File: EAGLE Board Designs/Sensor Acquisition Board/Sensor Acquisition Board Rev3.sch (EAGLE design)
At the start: 79 parts, among them J1 CONNECTOR-AVR-ISP__, J2 CONNECTOR-SENSOR_NF_S_RA_BLACK, J3 CONNECTOR-SENSOR_NF_S_RA_BLACK, J4 CONNECTOR-SENSOR_NF_S_RA_BLACK, J5 CONNECTOR-SENSOR_NF_S_RA_BLACK, J6 CONNECTOR-CAN_NF_S_RA_BLACK, U1 LM340, U10 OPAMP_1_CHANNEL_OPA991, U11 OPAMP_1_CHANNEL_OPA991, U12 OPAMP_1_CHANNEL_OPA991, U13 OPAMP_1_CHANNEL_OPA991, U2 ATMEGA328P-AU, U3 MCP2515, U4 MCP3204, U5 CAN_TRANSCIEVER_TCAN1051HQV-Q1, U6 MAX7400, U7 MAX7400, U8 MAX7400, U9 MAX7400, X1 CRYSTAL16MHZ, X2 CRYSTAL16MHZ

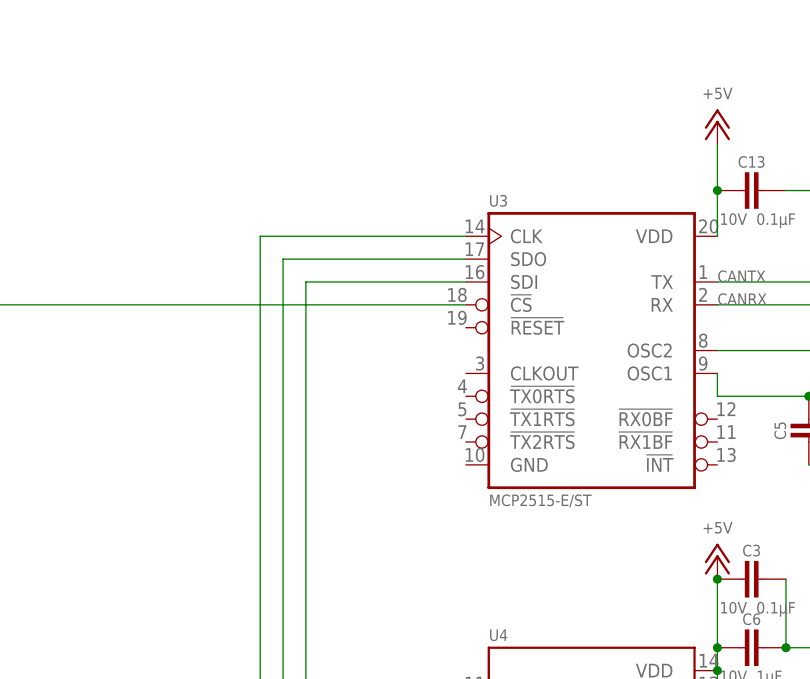
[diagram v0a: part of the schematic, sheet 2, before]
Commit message: Fixed resetlow on MCP2515
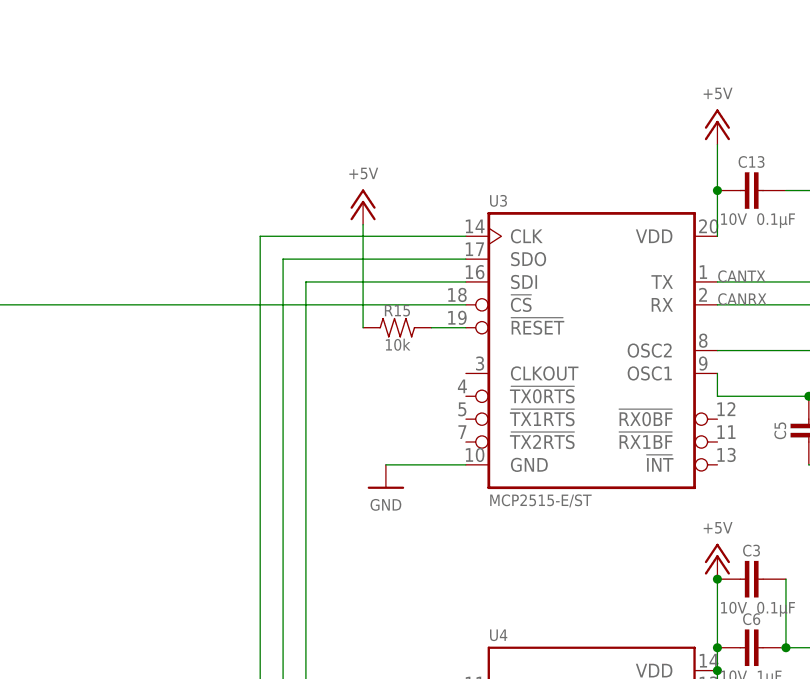
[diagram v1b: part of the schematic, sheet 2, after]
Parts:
- added R15: RESISTOR_0603_10K, HyTechDevices:RESISTOR_0603_10K
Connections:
- new net N$5: R15.2, U3.!RESET
- net +5V: now also R15.1
- net GND: now also U3.GND
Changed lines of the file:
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@@
 <part name="GND12" library="HyTechSupplies" deviceset="GND" device=""/>
 <part name="U$7" library="HyTechFrames" deviceset="FRAME_B" device=""/>
+<part name="R15" library="HyTechDevices" deviceset="RESISTOR_?_*" device="0603" technology="10K"/>
+<part name="P1" library="HyTechSupplies" deviceset="+5V" device=""/>
+<part name="P2" library="HyTechSupplies" deviceset="GND" device=""/>
 </parts>
 <sheets>
@@
 <attribute name="SHEET" x="411.48" y="2.54" size="2.54" layer="94"/>
 </instance>
+<instance part="R15" gate="G$1" x="130.81" y="193.04" smashed="yes">
+<attribute name="NAME" x="129.54" y="194.31" size="1.27" layer="95" align="bottom-center"/>
+<attribute name="RESISTANCE" x="129.54" y="191.77" size="1.27" layer="96" align="top-center"/>
+</instance>
+<instance part="P1" gate="1" x="125.73" y="207.01" smashed="yes">
+<attribute name="VALUE" x="125.73" y="209.55" size="1.27" layer="96" align="bottom-center"/>
+</instance>
+<instance part="P2" gate="1" x="128.27" y="175.26" smashed="yes">
+<attribute name="VALUE" x="128.27" y="173.99" size="1.27" layer="96" align="top-center"/>
+</instance>
 </instances>
 <busses>
@@
 <pinref part="GND12" gate="1" pin="GND"/>
 <wire x1="215.9" y1="165.1" x2="215.9" y2="162.56" width="0.1524" layer="91"/>
+</segment>
+<segment>
+<pinref part="U3" gate="G$1" pin="GND"/>
+<pinref part="P2" gate="1" pin="GND"/>
+<wire x1="137.16" y1="177.8" x2="128.27" y2="177.8" width="0.1524" layer="91"/>
 </segment>
 </net>
@@
 <pinref part="P+8" gate="1" pin="+5V"/>
 </segment>
+<segment>
+<pinref part="P1" gate="1" pin="+5V"/>
+<pinref part="R15" gate="G$1" pin="1"/>
+<wire x1="125.73" y1="204.47" x2="125.73" y2="193.04" width="0.1524" layer="91"/>
+</segment>
 </net>
 <net name="RESET" class="0">
@@
 </segment>
 </net>
+<net name="N$5" class="0">
+<segment>
+<pinref part="U3" gate="G$1" pin="!RESET"/>
+<pinref part="R15" gate="G$1" pin="2"/>
+<wire x1="137.16" y1="193.04" x2="133.35" y2="193.04" width="0.1524" layer="91"/>
+</segment>
+</net>

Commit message: SAB Rev3 Schematic and Board done, awaiting formal review
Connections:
- net ATMEGA_SDI: now also J1.SDI; no longer J1.SDO
- net ATMEGA_SDO: now also J1.SDO; no longer J1.SDI
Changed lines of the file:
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@@
 <pinref part="U2" gate="G$1" pin="(PWM/SDO)11"/>
 <wire x1="71.12" y1="147.32" x2="119.38" y2="147.32" width="0.1524" layer="91"/>
-<pinref part="J1" gate="G$1" pin="SDI"/>
-<wire x1="137.16" y1="119.38" x2="119.38" y2="119.38" width="0.1524" layer="91"/>
-<wire x1="119.38" y1="119.38" x2="119.38" y2="147.32" width="0.1524" layer="91"/>
+<wire x1="119.38" y1="121.92" x2="119.38" y2="147.32" width="0.1524" layer="91"/>
 <pinref part="U4" gate="G$1" pin="SDI"/>
 <wire x1="119.38" y1="147.32" x2="137.16" y2="147.32" width="0.1524" layer="91"/>
@@
 <wire x1="119.38" y1="147.32" x2="119.38" y2="198.12" width="0.1524" layer="91"/>
 <wire x1="119.38" y1="198.12" x2="137.16" y2="198.12" width="0.1524" layer="91"/>
+<pinref part="J1" gate="G$1" pin="SDO"/>
+<wire x1="119.38" y1="121.92" x2="137.16" y2="121.92" width="0.1524" layer="91"/>
 </segment>
 </net>
@@
 <wire x1="121.92" y1="149.86" x2="116.84" y2="149.86" width="0.1524" layer="91"/>
 <wire x1="116.84" y1="149.86" x2="71.12" y2="149.86" width="0.1524" layer="91"/>
-<wire x1="121.92" y1="149.86" x2="121.92" y2="121.92" width="0.1524" layer="91"/>
+<wire x1="121.92" y1="149.86" x2="121.92" y2="119.38" width="0.1524" layer="91"/>
 <junction x="121.92" y="149.86"/>
-<pinref part="J1" gate="G$1" pin="SDO"/>
-<wire x1="121.92" y1="121.92" x2="137.16" y2="121.92" width="0.1524" layer="91"/>
 <pinref part="U4" gate="G$1" pin="SDO"/>
 <wire x1="137.16" y1="149.86" x2="121.92" y2="149.86" width="0.1524" layer="91"/>
@@
 <wire x1="116.84" y1="200.66" x2="137.16" y2="200.66" width="0.1524" layer="91"/>
 <junction x="116.84" y="149.86"/>
+<pinref part="J1" gate="G$1" pin="SDI"/>
+<wire x1="121.92" y1="119.38" x2="137.16" y2="119.38" width="0.1524" layer="91"/>
 </segment>
 </net>

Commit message: Completed shipping version of rev3
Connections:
- net ATMEGA_SDI: now also J1.SDO; no longer J1.SDI
- net ATMEGA_SDO: now also J1.SDI; no longer J1.SDO
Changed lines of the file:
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@@
 <layers>
 <layer number="1" name="Top" color="4" fill="1" visible="no" active="no"/>
+<layer number="2" name="Route2" color="1" fill="3" visible="no" active="no"/>
+<layer number="3" name="Route3" color="4" fill="3" visible="no" active="no"/>
+<layer number="4" name="Route4" color="1" fill="4" visible="no" active="no"/>
+<layer number="5" name="Route5" color="4" fill="4" visible="no" active="no"/>
+<layer number="6" name="Route6" color="1" fill="8" visible="no" active="no"/>
+<layer number="7" name="Route7" color="4" fill="8" visible="no" active="no"/>
+<layer number="8" name="Route8" color="1" fill="2" visible="no" active="no"/>
+<layer number="9" name="Route9" color="4" fill="2" visible="no" active="no"/>
+<layer number="10" name="Route10" color="1" fill="7" visible="no" active="no"/>
+<layer number="11" name="Route11" color="4" fill="7" visible="no" active="no"/>
+<layer number="12" name="Route12" color="1" fill="5" visible="no" active="no"/>
+<layer number="13" name="Route13" color="4" fill="5" visible="no" active="no"/>
+<layer number="14" name="Route14" color="1" fill="6" visible="no" active="no"/>
+<layer number="15" name="Route15" color="4" fill="6" visible="no" active="no"/>
 <layer number="16" name="Bottom" color="1" fill="1" visible="no" active="no"/>
 <layer number="17" name="Pads" color="2" fill="1" visible="no" active="no"/>
@@
 <instance part="J6" gate="G$1" x="294.64" y="203.2" smashed="yes" rot="MR0">
 <attribute name="NAME" x="294.64" y="203.835" size="1.27" layer="95" rot="MR0"/>
-<attribute name="MODEL" x="294.64" y="189.865" size="1.27" layer="96" rot="MR0" align="top-left"/>
 </instance>
 <instance part="GND36" gate="1" x="271.78" y="205.74" smashed="yes">
@@
 <instance part="J2" gate="G$1" x="25.4" y="88.9" smashed="yes">
 <attribute name="NAME" x="25.4" y="89.535" size="1.27" layer="95"/>
-<attribute name="MODEL" x="25.4" y="75.565" size="1.27" layer="96" align="top-left"/>
 </instance>
 <instance part="P+5" gate="1" x="38.1" y="88.9" smashed="yes">
@@
 <instance part="J3" gate="G$1" x="25.4" y="40.64" smashed="yes">
 <attribute name="NAME" x="25.4" y="41.275" size="1.27" layer="95"/>
-<attribute name="MODEL" x="25.4" y="27.305" size="1.27" layer="96" align="top-left"/>
 </instance>
 <instance part="P+29" gate="1" x="38.1" y="40.64" smashed="yes">
@@
 <instance part="J4" gate="G$1" x="139.7" y="88.9" smashed="yes">
 <attribute name="NAME" x="139.7" y="89.535" size="1.27" layer="95"/>
-<attribute name="MODEL" x="139.7" y="75.565" size="1.27" layer="96" align="top-left"/>
 </instance>
 <instance part="P+33" gate="1" x="152.4" y="88.9" smashed="yes">
@@
 <instance part="J5" gate="G$1" x="139.7" y="40.64" smashed="yes">
 <attribute name="NAME" x="139.7" y="41.275" size="1.27" layer="95"/>
-<attribute name="MODEL" x="139.7" y="27.305" size="1.27" layer="96" align="top-left"/>
 </instance>
 <instance part="P+37" gate="1" x="152.4" y="40.64" smashed="yes">
@@
 <pinref part="U2" gate="G$1" pin="(PWM/SDO)11"/>
 <wire x1="71.12" y1="147.32" x2="119.38" y2="147.32" width="0.1524" layer="91"/>
-<wire x1="119.38" y1="121.92" x2="119.38" y2="147.32" width="0.1524" layer="91"/>
+<wire x1="119.38" y1="119.38" x2="119.38" y2="147.32" width="0.1524" layer="91"/>
 <pinref part="U4" gate="G$1" pin="SDI"/>
 <wire x1="119.38" y1="147.32" x2="137.16" y2="147.32" width="0.1524" layer="91"/>
@@
 <wire x1="119.38" y1="147.32" x2="119.38" y2="198.12" width="0.1524" layer="91"/>
 <wire x1="119.38" y1="198.12" x2="137.16" y2="198.12" width="0.1524" layer="91"/>
-<pinref part="J1" gate="G$1" pin="SDO"/>
-<wire x1="119.38" y1="121.92" x2="137.16" y2="121.92" width="0.1524" layer="91"/>
+<pinref part="J1" gate="G$1" pin="SDI"/>
+<wire x1="137.16" y1="119.38" x2="119.38" y2="119.38" width="0.1524" layer="91"/>
 </segment>
 </net>
@@
 <segment>
 <pinref part="U2" gate="G$1" pin="(SDI)12"/>
-<wire x1="121.92" y1="149.86" x2="116.84" y2="149.86" width="0.1524" layer="91"/>
 <wire x1="116.84" y1="149.86" x2="71.12" y2="149.86" width="0.1524" layer="91"/>
-<wire x1="121.92" y1="149.86" x2="121.92" y2="119.38" width="0.1524" layer="91"/>
-<junction x="121.92" y="149.86"/>
 <pinref part="U4" gate="G$1" pin="SDO"/>
 <wire x1="137.16" y1="149.86" x2="121.92" y2="149.86" width="0.1524" layer="91"/>
 <label x="71.12" y="149.86" size="1.27" layer="95"/>
 <pinref part="U3" gate="G$1" pin="SDO"/>
+<wire x1="121.92" y1="149.86" x2="116.84" y2="149.86" width="0.1524" layer="91"/>
 <wire x1="116.84" y1="149.86" x2="116.84" y2="200.66" width="0.1524" layer="91"/>
 <wire x1="116.84" y1="200.66" x2="137.16" y2="200.66" width="0.1524" layer="91"/>
 <junction x="116.84" y="149.86"/>
-<pinref part="J1" gate="G$1" pin="SDI"/>
-<wire x1="121.92" y1="119.38" x2="137.16" y2="119.38" width="0.1524" layer="91"/>
+<pinref part="J1" gate="G$1" pin="SDO"/>
+<wire x1="137.16" y1="121.92" x2="121.92" y2="121.92" width="0.1524" layer="91"/>
+<wire x1="121.92" y1="121.92" x2="121.92" y2="149.86" width="0.1524" layer="91"/>
+<junction x="121.92" y="149.86"/>
 </segment>
 </net>
